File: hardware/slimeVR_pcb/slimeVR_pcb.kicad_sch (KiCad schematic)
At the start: 31 parts, among them J1 USB_C_Receptacle_USB2.0_16P, Q1 Q_Dual_NMOS_S1G1S2G2D2D2D1D1, SW1 SW_SPDT, SW2 SW_Push, SW3 SW_Push, U1 ESP32-S2-WROVER, U10 AP2112K-3.3, U2 TP4057, U3 BMI160, U4 ICM-20948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

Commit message: stuff
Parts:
- removed U3: BMI160, Package_LGA:Bosch_LGA-14_3x2.5mm_P0.5mm, symbol Sensor_Motion:BMI160
- removed U4: ICM-20948, Sensor_Motion:InvenSense_QFN-24_3x3mm_P0.4mm, symbol Sensor_Motion:ICM-20948
- removed U5: MPU-9250, Sensor_Motion:InvenSense_QFN-24_3x3mm_P0.4mm, symbol Sensor_Motion:MPU-9250
- removed U6: MPU-6050, Sensor_Motion:InvenSense_QFN-24_4x4mm_P0.5mm, symbol Sensor_Motion:MPU-6050
- removed U9: MMC5883MA, Package_LGA:LGA-16_3x3mm_P0.5mm, symbol Sensor_Magnetic:MMC5883MA
- added C2, C3: 100n, Capacitor_SMD:C_0603_1608Metric_Pad1.08x0.95mm_HandSolder, symbol Device:C
- added C4: 1u, Capacitor_SMD:C_0603_1608Metric_Pad1.08x0.95mm_HandSolder, symbol Device:C
- added JP1: SolderJumper_2_Open, Jumper:SolderJumper-2_P1.3mm_Open_TrianglePad1.0x1.5mm, symbol Jumper:SolderJumper_2_Open
- added R12, R13: 1k, Resistor_SMD:R_0603_1608Metric_Pad0.98x0.95mm_HandSolder, symbol Device:R
- added U3: ICM-45686, easyeda2kicad:LGA-14_L3.0-W2.5-P0.50-TL, symbol easyeda2kicad:ICM-45686
- added U4: LSM6DSRTR, easyeda2kicad:LGA-14_L3.0-W2.5-P0.50-BR, symbol easyeda2kicad:LSM6DSRTR
- added U5: QMC6309, easyeda2kicad:X1-WLB0808-4_L0.8-W0.8-P0.40-TL, symbol easyeda2kicad:QMC6309
- R8, R9: value 1k -> 5k1
- SW1: footprint Button_Switch_THT:SW_Slide_SPDT_Straight_CK_OS102011MS2Q -> Button_Switch_THT:SW_Slide_SPDT_Angled_CK_OS102011MA1Q
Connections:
- net +3V3: now also C2.1, C3.1, C4.1, R12.1, R13.1, U3.12 (AP_CS), U3.5 (VDDIO), U3.8 (VDD), U4.12 (CS), U4.5 (VDDIO), U4.8 (VDD), U5.B1 (VDD)
- net +5V: now also JP1.1 (A); no longer SW1.1 (A)
- net +BATT: now also R2.2; no longer R2.1
- net GND: now also C2.2, C3.2, C4.2, U3.1 (AP_SDO/AP_AD0), U3.6 (GND), U4.1 (SDO/SA0), U4.6 (GND), U4.7 (GND), U5.A1 (VSS)
- net SCL: now also R13.2, U3.13 (AP_SCL/AP_SCLK), U4.13 (SCL)
- net SDA: now also R12.2, U3.14 (AP_SDA/AP_SDIO/AP_SDI), U4.14 (SDA)
- net at Q1.5 (D), Q1.7 (D): now also Q1.6 (D), Q1.8 (D)
- net at C1.1, U7.5 (VCC): now also R2.1; no longer R2.2
- new net: JP1.2 (B), SW1.1 (A)
- new net INT: U3.4 (INT1/INT), U4.4 (INT1)
- new net SCL_IMU: U3.3 (RESV/AUX1_SCLK/MAS_CLK), U4.3 (SCX), U5.A2 (SCL)
- new net SDA_IMU: U3.2 (RESV/AUX1_SDIO/AUX1_SDI/MAS_DA), U4.2 (SDX), U5.B2 (SDA)
- no-connect marks 0 -> 7
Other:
- note added: "TODO: - ICM-45686 IMU - LSM6DSR IMU - QMC6309 mag (useable by either IMU)"
- note added: "TODO: verify BAT_* never over 3.3V"
- moved on the sheet: R2

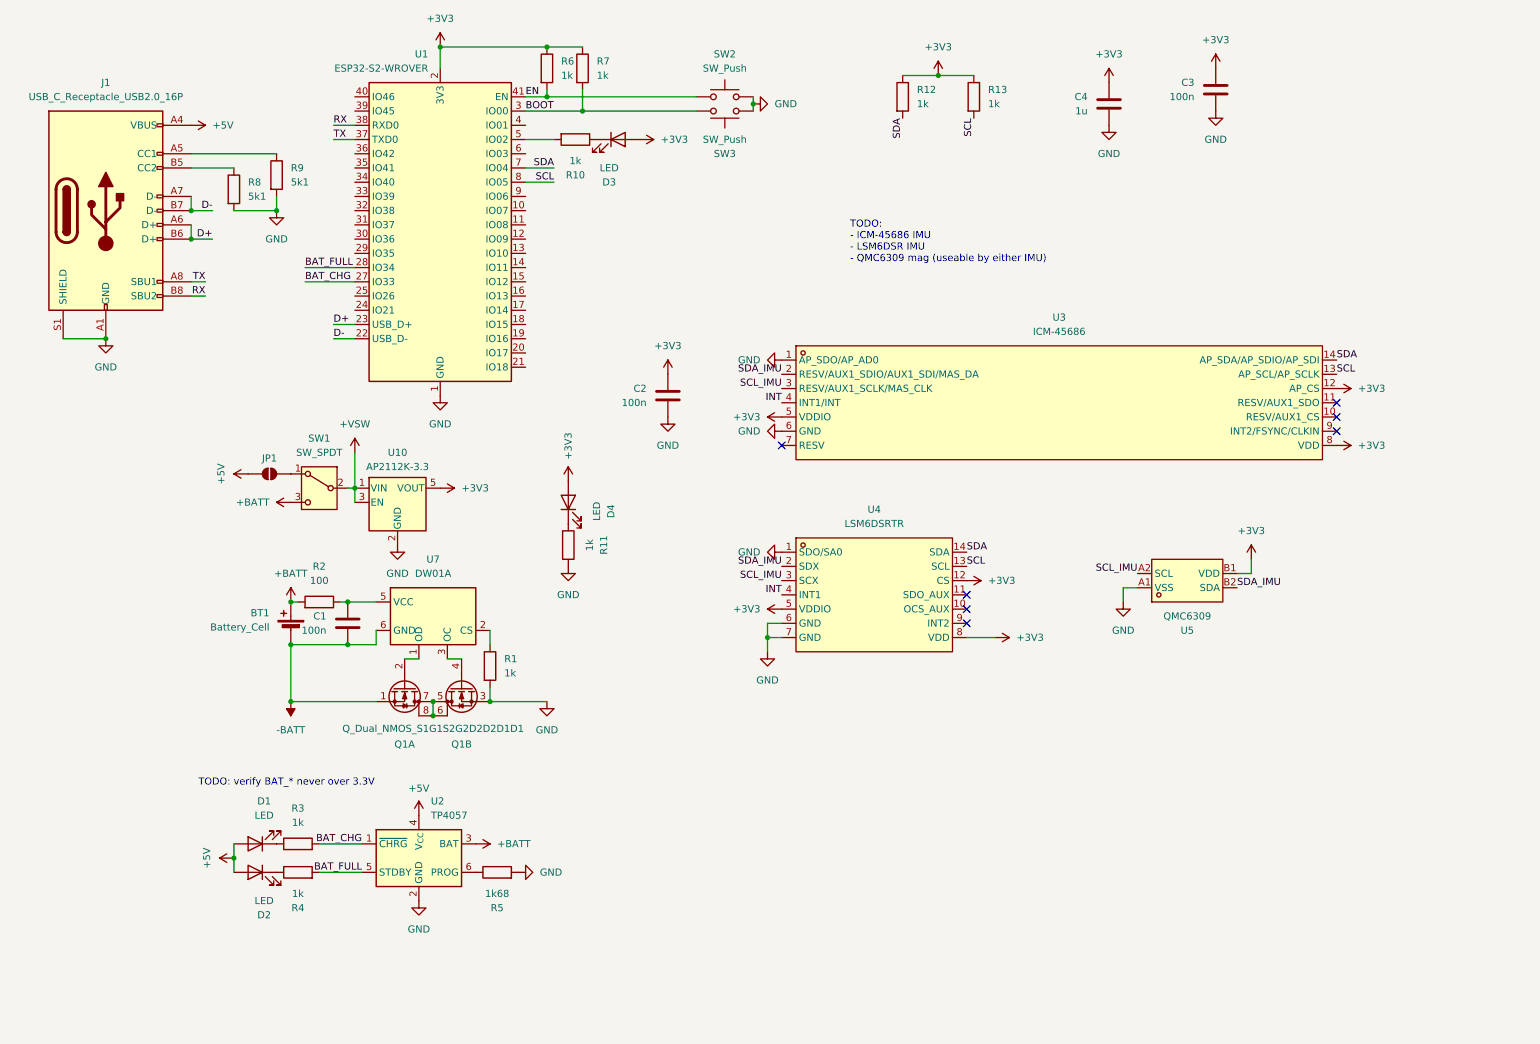
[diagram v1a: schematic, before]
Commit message: continue pcb, cleanup schematic
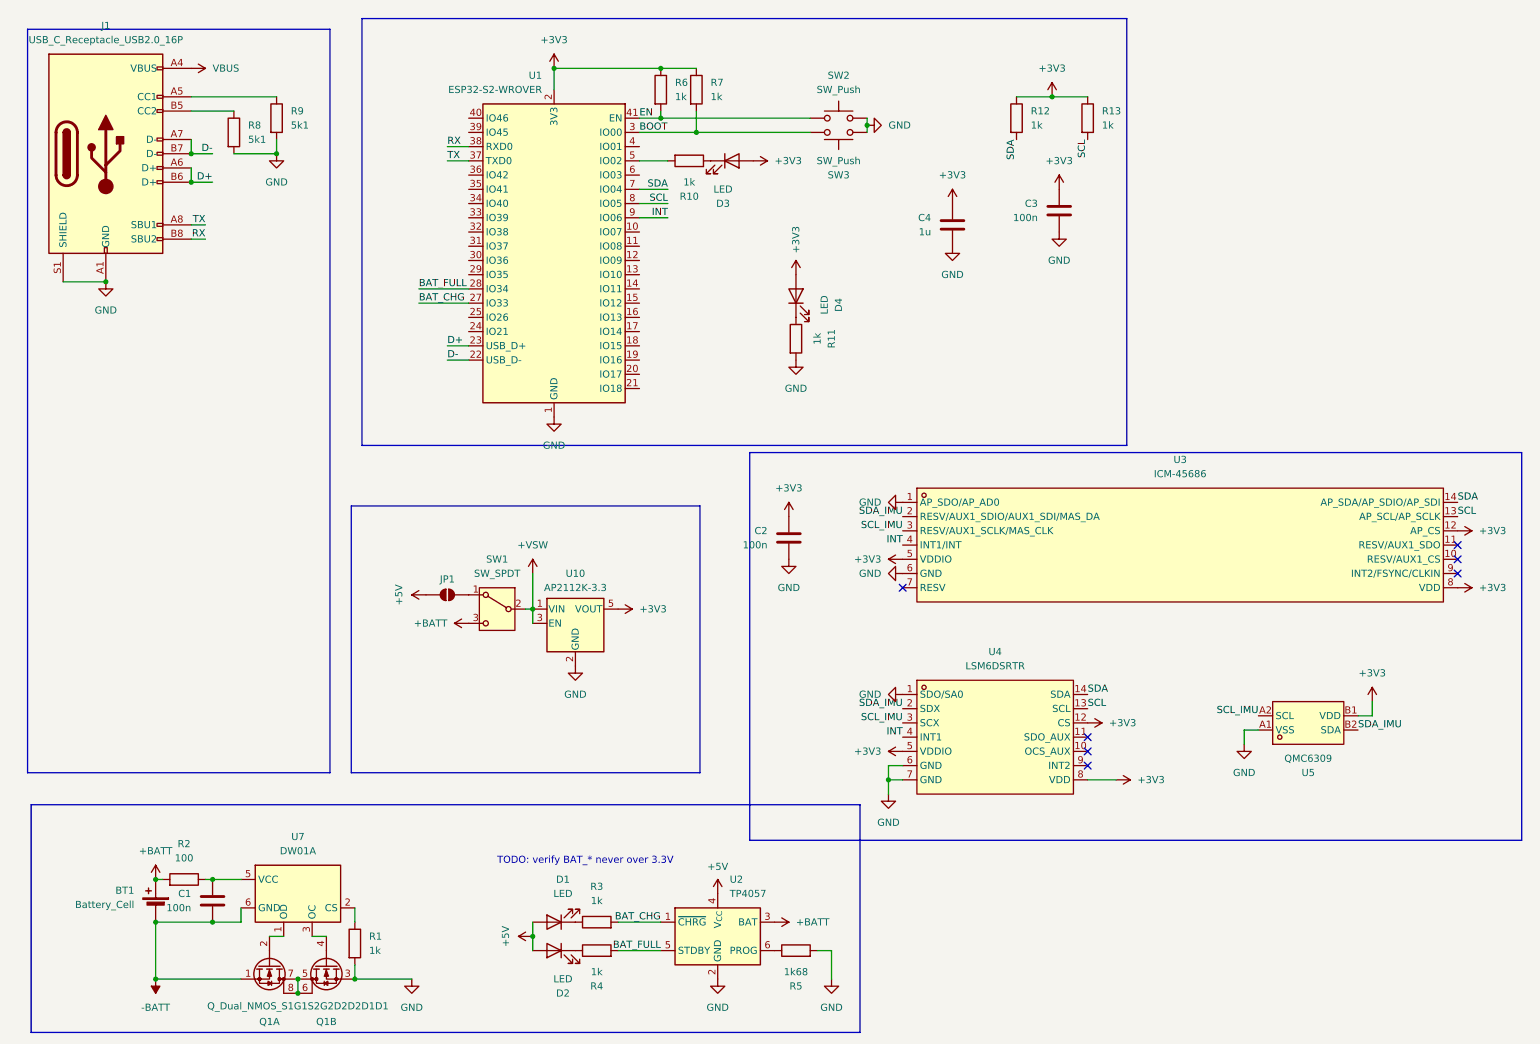
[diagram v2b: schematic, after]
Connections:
- net +5V: no longer J1.A4 (VBUS), J1.A9 (VBUS), J1.B4 (VBUS), J1.B9 (VBUS)
- net INT: now also U1.9 (IO06)
- new net VBUS: J1.A4 (VBUS), J1.A9 (VBUS), J1.B4 (VBUS), J1.B9 (VBUS)
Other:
- note removed: "TODO: - ICM-45686 IMU - LSM6DSR IMU - QMC6309 mag (useable by either IMU)"
- moved on the sheet: BT1, C1, C2, C3, C4, D1, D2, D3, D4, J1, JP1, Q1A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

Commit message: add protection circuit
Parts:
- added JP2: SolderJumper_2_Open, Jumper:SolderJumper-2_P1.3mm_Open_TrianglePad1.0x1.5mm, symbol Jumper:SolderJumper_2_Open
- added R14: 330k, Resistor_SMD:R_0603_1608Metric_Pad0.98x0.95mm_HandSolder, symbol Device:R
- added R15: 150k, Resistor_SMD:R_0603_1608Metric_Pad0.98x0.95mm_HandSolder, symbol Device:R
- added U6: TPS25200DRVR, Package_SON:WSON-6-1EP_2x2mm_P0.65mm_EP1x1.6mm_ThermalVias, symbol slime_parts:TPS25200DRVR
- R6, R7: now not fitted; now left out of the parts list
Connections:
- net +5V: now also JP2.2 (B), U6.1 (OUT)
- net GND: now also R15.2, U6.5 (GND), U6.7 (EP)
- net VBUS: now also JP2.1 (A), R14.1, U6.6 (IN)
- new net: R14.2, U6.4 (EN)
- new net: R15.1, U6.2 (ILIM)
- no-connect marks 7 -> 8

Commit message: cleanup pcb
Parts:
- removed R6: 1k, Resistor_SMD:R_0603_1608Metric_Pad0.98x0.95mm_HandSolder, symbol Device:R
- removed SW2: SW_Push, Button_Switch_SMD:SW_Push_1P1T_XKB_TS-1187A, symbol Switch:SW_Push
- added TP1: GND, TestPoint:TestPoint_Pad_4.0x4.0mm, symbol Connector:TestPoint
- added TP2: +5V, TestPoint:TestPoint_Pad_4.0x4.0mm, symbol Connector:TestPoint
- D1: value LED -> red
- D2: value LED -> blue
- D3: value LED -> green
- D4: value LED -> white
- SW3: footprint Button_Switch_SMD:SW_Push_1P1T_XKB_TS-1187A -> Button_Switch_SMD:SW_Push_1P1T_NO_CK_KSC7xxJ
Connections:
- net EN is gone; now on net +3V3: U1.41 (EN)
- net +5V: now also TP2.1
- net GND: now also U3.7 (RESV), TP1.1
- no-connect marks 8 -> 7
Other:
- moved on the sheet: C2, C3, C4, D4, R11, SW3

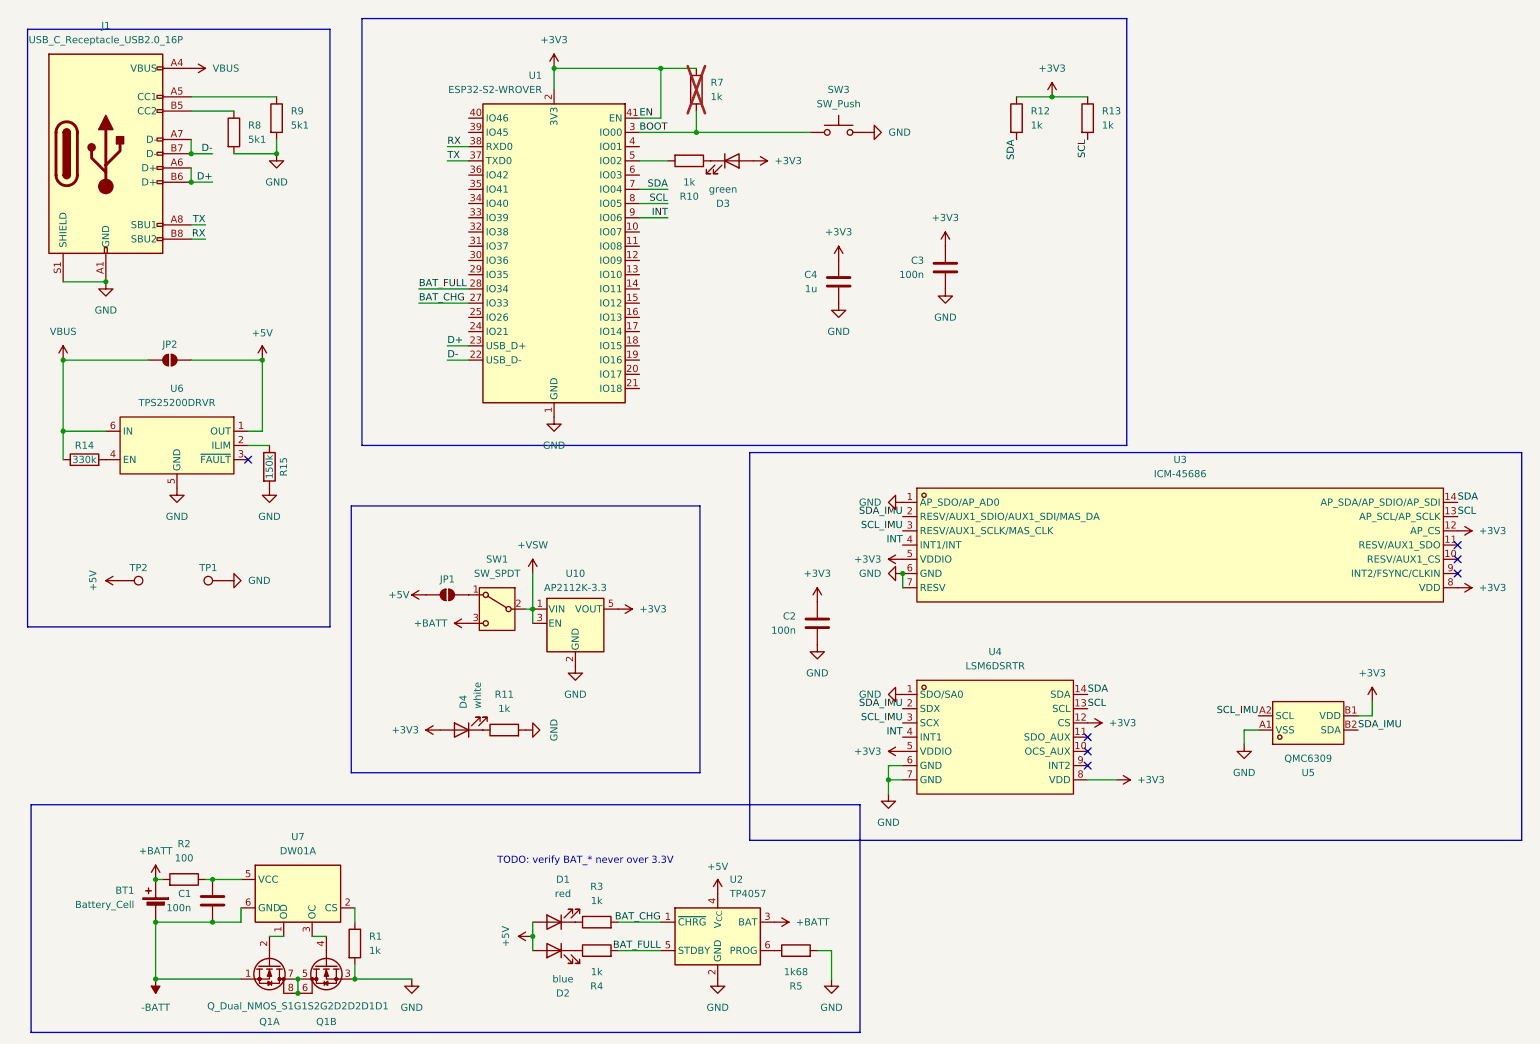
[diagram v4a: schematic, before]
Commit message: routed IMU
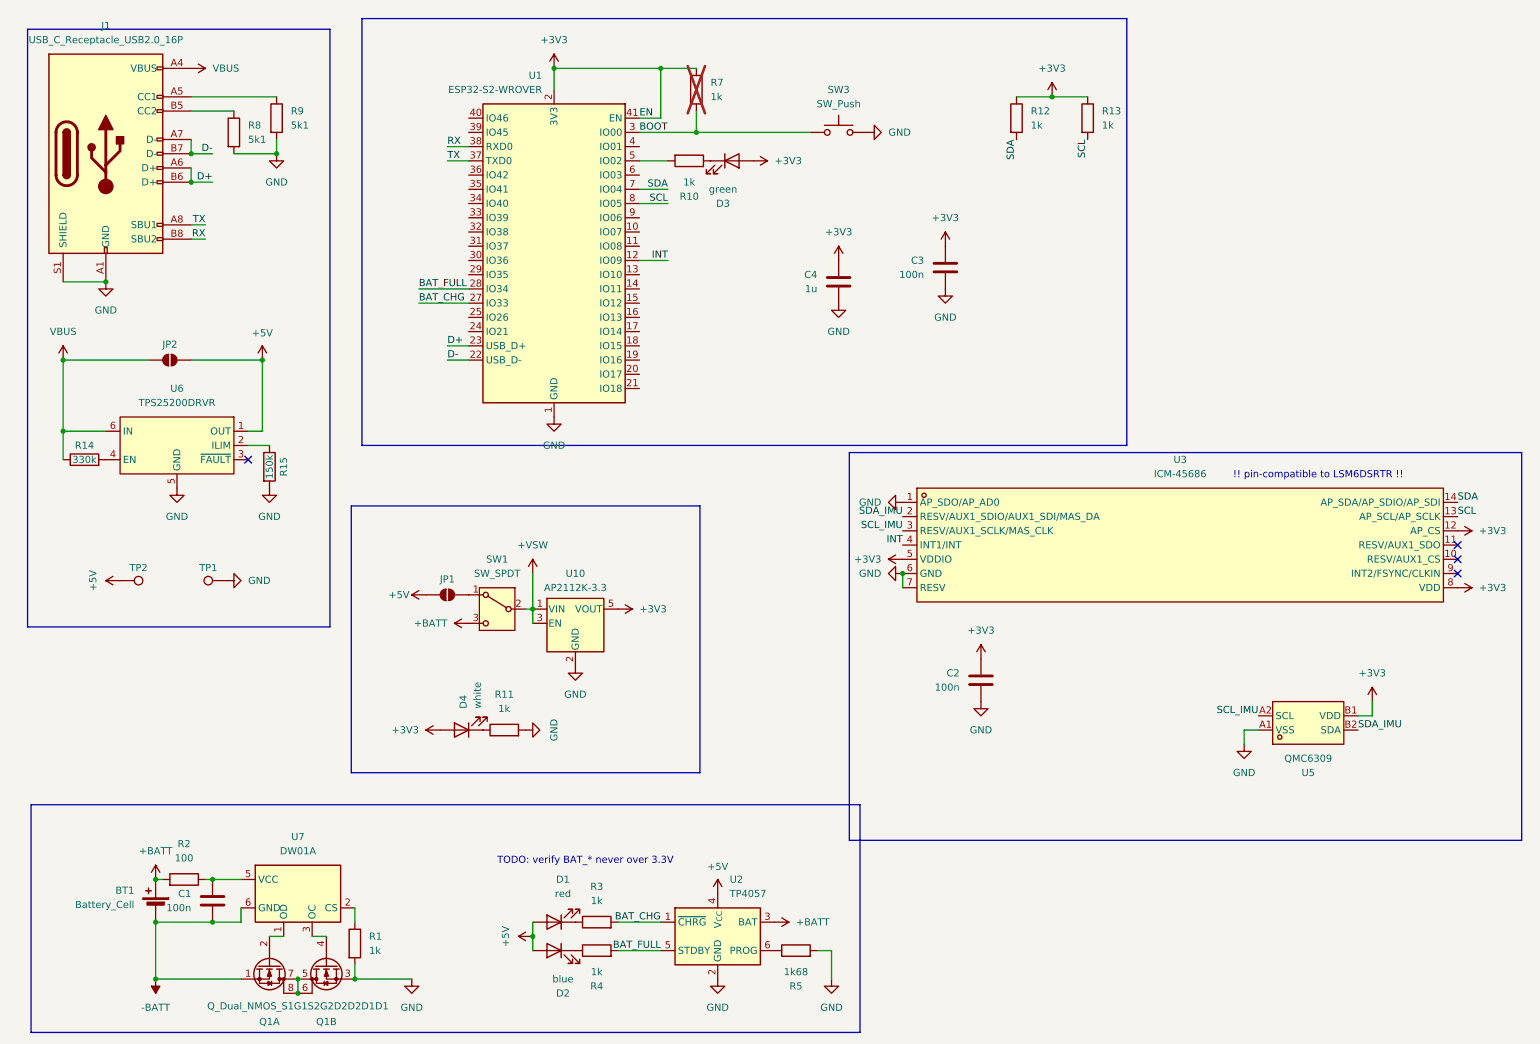
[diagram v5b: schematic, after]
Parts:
- removed U4: LSM6DSRTR, easyeda2kicad:LGA-14_L3.0-W2.5-P0.50-BR, symbol easyeda2kicad:LSM6DSRTR
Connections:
- net INT: now also U1.12 (IO09); no longer U1.9 (IO06)
- no-connect marks 7 -> 4
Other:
- note added: "!! pin-compatible to LSM6DSRTR !!"
- moved on the sheet: C2

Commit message: fix DRC, cleanup
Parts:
- U6: footprint Package_SON:WSON-6-1EP_2x2mm_P0.65mm_EP1x1.6mm_ThermalVias -> Package_SON:WSON-6-1EP_2x2mm_P0.65mm_EP1x1.6mm
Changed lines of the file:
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@@
 			)
 		)
-		(property "Footprint" "Package_SON:WSON-6-1EP_2x2mm_P0.65mm_EP1x1.6mm_ThermalVias"
+		(property "Footprint" "Package_SON:WSON-6-1EP_2x2mm_P0.65mm_EP1x1.6mm"
 			(at 41.91 101.6 0)
 			(effects

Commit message: tiredly add testpads
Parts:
- added TP3: SDA, TestPoint:TestPoint_Pad_D1.0mm, symbol Connector:TestPoint
- added TP4: SCL, TestPoint:TestPoint_Pad_D1.0mm, symbol Connector:TestPoint
- added TP5: INT, TestPoint:TestPoint_Pad_D1.0mm, symbol Connector:TestPoint
- added TP6: iSDA, TestPoint:TestPoint_Pad_D1.0mm, symbol Connector:TestPoint
- added TP7: iSCL, TestPoint:TestPoint_Pad_D1.0mm, symbol Connector:TestPoint
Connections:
- net INT: now also TP5.1
- net SCL: now also TP4.1
- net SCL_IMU: now also TP7.1
- net SDA: now also TP3.1
- net SDA_IMU: now also TP6.1
